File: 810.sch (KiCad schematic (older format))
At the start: 286 parts

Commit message: changed to Toshiba matched pairs, added 12dB/24dB selector switch
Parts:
- removed Q? (x2): PMP4201G, TO_SOT_Packages_SMD:SOT-353, symbol PMP4201G
- removed Q? (x2): PMP5201G, TO_SOT_Packages_SMD:SOT-353_SC-70-5, symbol PMP5201G
- added Q? (x2): 2SA1618, TO_SOT_Packages_SMD:SOT-353_SC-70-5, symbol 2SA1618
- added Q? (x2): 2SC4207, TO_SOT_Packages_SMD:SOT-353_SC-70-5, symbol 2SC4207
- added R?: 68K, MyModules:SM0603-R-JRL, symbol R_US
- added SW?: SPDT, symbol SPDT
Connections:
- wire segments 594 -> 596
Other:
- note added: "VCA"
- moved on the sheet: C?, J?, Q?, R?, SW?, TP?, U?, U?A, U?B, VR?

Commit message: gibber jabber
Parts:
- removed C?: 10μ, symbol CP_US
- removed U?: CD40106, Housings_SSOP:TSSOP-14_4.4x5mm_Pitch0.65mm, symbol CD40106
- added C?: 10μF, Capacitors_SMD:c_elec_5x5.3, symbol CP_US
- added J?: PJ301BM, symbol JACK_MONO_SW
- added U?: CD40106, Housings_SSOP:TSSOP-14_4.4x5mm_Pitch0.65mm, symbol CD40106
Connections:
- net +12V: now also U?.10 (J), U?.11 (K); no longer U?.5 (K), U?.6 (J)
- net GND: now also U?.11 (In), U?.13 (In), U?.5 (In), U?.9 (In), U?.9 (Sd), J?.1; no longer U?.1 (In), U?.1 (In), U?.1 (In), U?.1 (In), U?.7 (Sd), U?.8 (VSS)
- net VCO_PULSE: now also U?.12 (X0)
- net VCO_SAW: now also U?.14 (X1)
- net VCO_SINE: now also U?.11 (X3)
- net VCO_TRI: now also U?.15 (X2)
- net at C?.1, R?.1, U?.3 (-): now also C?.1 (+)
- net at R?.2, R?.2: now also C?.2 (-)
- net at U?.9 (B): now also U?.15 (Q); no longer U?.1 (Q)
- net at C?.1, R?.1, R?.1: now also U?.3 (In)
- net at U?.2 (~Q): now also U?.13 (Cp); no longer U?.3 (Cp)
- net at U?.3 (Cp): now also U?.4 (Out)
- net at U?.2 (Out), U?.4 (Cd): now also U?.12 (Cd); no longer U?.4 (Cd)
- net SYNC_IN: no longer names the net of R?.1
- net SYNC_IN: now also J?.3
- no-connect marks 24 -> 25
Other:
- note added: "00 PULSE\n01 SAW\n10 TRI\n11 SINE"
- note added: "SYNC"
- note removed: "00 LOW PASS 24 dB\n01 LOW PASS 12 dB\n10 BAND PASS 12 dB\n11 HIGH PASS 24 dB"
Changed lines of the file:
@@
 	0    -1   -1   0
 $EndComp
-Text GLabel 20275 5575 0    60   Input ~ 0
+Text GLabel 19975 5575 0    60   Input ~ 0
 VCO_TRI
 Text GLabel 20125 5275 0    60   Input ~ 0
 VCO_PULSE
-Text GLabel 20275 5725 0    60   Input ~ 0
+Text GLabel 20050 5725 0    60   Input ~ 0
 VCO_SINE
-Text GLabel 20175 5425 0    60   Input ~ 0
+Text GLabel 20025 5425 0    60   Input ~ 0
 VCO_SAW
 Text GLabel 21975 5275 2    60   Output ~ 0
@@
 	0    -1   -1   0
 $EndComp
-Text GLabel 1425 6875 0    60   Input ~ 0
-SYNC_IN
 Wire Wire Line
 	1900 6875 1950 6875
@@
 Wire Wire Line
 	2025 11975 2425 11975
-$Comp
-L CP_US C?
-U 1 1 596C3983
-P 3275 13125
-F 0 "C?" V 3350 12900 50  0000 L CNN
-F 1 "10μ" V 3350 13200 50  0000 L CNN
-F 2 "" H 3275 13125 60  0000 C CNN
-F 3 "" H 3275 13125 60  0000 C CNN
-	1    3275 13125
-	0    1    1    0
-$EndComp
 Wire Wire Line
 	4675 13225 5425 13225
@@
 $Comp
 L CD4027 U?
-U 1 1 596C393E
+U 2 1 596C393E
 P 23350 4575
 F 0 "U?" H 23550 4875 60  0000 C CNN
@@
 F 2 "Housings_SSOP:TSSOP-16_4.4x5mm_Pitch0.65mm" H 23350 4575 60  0001 C CNN
 F 3 "" H 23350 4575 60  0000 C CNN
-	1    23350 4575
+	2    23350 4575
 	-1   0    0    -1
 $EndComp
-Text Notes 22300 2975 0    60   ~ 0
-00 LOW PASS 24 dB\n01 LOW PASS 12 dB\n10 BAND PASS 12 dB\n11 HIGH PASS 24 dB
+Text Notes 22275 4100 0    60   ~ 0
+00 PULSE\n01 SAW\n10 TRI\n11 SINE
 $Comp
 L +12V #PWR?
@@
 $Comp
 L CD40106 U?
-U 1 1 596C3983
+U 2 1 596C3983
 P 26750 4575
 F 0 "U?" H 26850 4725 50  0000 L CNN
@@
 F 2 "Housings_SSOP:TSSOP-14_4.4x5mm_Pitch0.65mm" H 26750 4575 60  0001 C CNN
 F 3 "" H 26750 4575 60  0000 C CNN
-	1    26750 4575
+	2    26750 4575
 	-1   0    0    -1
 $EndComp
@@
 $Comp
 L CD40106 U?
-U 1 1 596C3991
+U 4 1 596C3991
 P 29625 3900
 F 0 "U?" H 29725 4050 50  0000 L CNN
@@
 F 2 "Housings_SSOP:TSSOP-14_4.4x5mm_Pitch0.65mm" H 29625 3900 60  0001 C CNN
 F 3 "" H 29625 3900 60  0000 C CNN
-	1    29625 3900
+	4    29625 3900
 	1    0    0    -1
 $EndComp
 $Comp
 L CD40106 U?
-U 1 1 596C3998
+U 5 1 596C3998
 P 29625 4600
 F 0 "U?" H 29725 4750 50  0000 L CNN
@@
 F 2 "Housings_SSOP:TSSOP-14_4.4x5mm_Pitch0.65mm" H 29625 4600 60  0001 C CNN
 F 3 "" H 29625 4600 60  0000 C CNN
-	1    29625 4600
+	5    29625 4600
 	1    0    0    -1
 $EndComp
 $Comp
 L CD40106 U?
-U 1 1 596C399F
+U 6 1 596C399F
 P 29625 5300
 F 0 "U?" H 29725 5450 50  0000 L CNN
@@
 F 2 "Housings_SSOP:TSSOP-14_4.4x5mm_Pitch0.65mm" H 29625 5300 60  0001 C CNN
 F 3 "" H 29625 5300 60  0000 C CNN
-	1    29625 5300
+	6    29625 5300
 	1    0    0    -1
 $EndComp
 $Comp
 L CD40106 U?
-U 1 1 596C39A6
+U 3 1 596C39A6
 P 29625 3250
 F 0 "U?" H 29725 3400 50  0000 L CNN
@@
 F 2 "Housings_SSOP:TSSOP-14_4.4x5mm_Pitch0.65mm" H 29625 3250 60  0001 C CNN
 F 3 "" H 29625 3250 60  0000 C CNN
-	1    29625 3250
+	3    29625 3250
 	1    0    0    -1
 $EndComp
@@
 Wire Wire Line
 	11725 14625 18850 14625
+$Comp
+L CP_US C?
+U 1 1 5971B5DE
+P 3275 13125
+F 0 "C?" V 3100 12925 50  0000 L CNN
+F 1 "10μF" V 3100 13150 50  0000 L CNN
+F 2 "Capacitors_SMD:c_elec_5x5.3" H 3275 13125 60  0001 C CNN
+F 3 "" H 3275 13125 60  0000 C CNN
+F 4 "UUQ1E100MCL1GB" V 3425 13225 60  0000 C CNN "Part Number"
+	1    3275 13125
+	0    1    1    0
+$EndComp
+Wire Wire Line
+	20125 5275 20350 5275
+Wire Wire Line
+	20025 5425 20350 5425
+Wire Wire Line
+	19975 5575 20350 5575
+Wire Wire Line
+	20050 5725 20350 5725
+$Comp
+L JACK_MONO_SW J?
+U 1 1 59733593
+P 1175 7025
+F 0 "J?" H 625 6925 60  0000 C CNN
+F 1 "PJ301BM" H 925 7225 60  0000 C CNN
+F 2 "" H 1075 7025 60  0000 C CNN
+F 3 "" H 1075 7025 60  0000 C CNN
+	1    1175 7025
+	1    0    0    1
+$EndComp
+$Comp
+L GND_R #PWR?
+U 1 1 59734986
+P 1425 7350
+F 0 "#PWR?" H 1425 7350 30  0001 C CNN
+F 1 "GND_R" H 1425 7250 30  0001 C CNN
+F 2 "" H 1425 7350 60  0000 C CNN
+F 3 "" H 1425 7350 60  0000 C CNN
+	1    1425 7350
+	1    0    0    -1
+$EndComp
+Wire Wire Line
+	1425 7175 1425 7350
+NoConn ~ 1425 7025
+Text Notes 900  6750 0    60   ~ 0
+SYNC
 $EndSCHEMATC

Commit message: finishing off, tidying up
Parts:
- removed SW?: DP6T-ROTARY-SWITCH, symbol DP6T-ROTARY-SWITCH
- added P?: CONN_01X08, Pin_Headers:Pin_Header_Angled_1x08_Pitch2.54mm, symbol CONN_01X08
- Q? (x2): footprint TO_SOT_Packages_SMD:SOT-353_SC-70-5 -> MyModules:SOT753_TSOP5_SC-74A
- SW?: value KS-01Q -> BF3-1050; footprint synth:KS-01Q-02-JRL -> MyModules:B3F-1050-OMRON
- VR?: footprint (none) -> MyModules:Bourns-3296W
- VR?: footprint (none) -> MyModules:RV16A-41-JRL
- VR?: footprint MyModules:TC33X-2 -> MyModules:Bourns-3296W
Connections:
- net +10V: now also R?.2, R?.2, VR?.1, VR?.3; no longer U?.8 (V+)
- net +12V: now also U?.8 (V+); no longer R?.2, R?.2, VR?.1, VR?.3
- net -10V: now also VR?.3; no longer U?.4 (V-)
- net -12V: now also U?.4 (V-); no longer VR?.3
- net GND: now also P?.6 (P6), P?.7 (P7)
- net at R?.1, VR?.1: now also P?.1 (P1)
- net at R?.1, R?.2: now also P?.2 (P2)
- net at R?.1, R?.2: now also P?.4 (P4)
- net at R?.1, R?.2: now also P?.5 (P5)
- net at R?.1, R?.2: now also P?.3 (P3)
- net at U?.1 (+): now also P?.8 (P8)
- net at VR?.2: now also R?.1
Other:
- note added: "Is additional DC\nblocking stage \nreally needed\nhere?"
- note added: "JP8 SYNC"
- note added: "ROTARY SWITCH\nGOES ON SUB BOARD"
- note added: "USE TOSHIBA\nNPN/PNP\nARRAY HERE?"

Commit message: added bi-color LED level indicator circuit
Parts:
- added C?: 0.047μF, symbol C_US
- added C?: 0.22µ, MyModules:SM0603-C-JRL, symbol C_US
- added D?: LED_BICOLOR, symbol LED_BICOLOR
- added D?: 1N4148, symbol D
- added R?: 100K, MyModules:SM0603-R-JRL, symbol R_US
- added R? (x2): 10K, MyModules:SM0603-R-JRL, symbol R_US
- added R?: 1meg, MyModules:SM0603-R-JRL, symbol R_US
- added R?: 1K, MyModules:SM0603-R-JRL, symbol R_US
- added R?: 51K, MyModules:SM0603-R-JRL, symbol R_US
- added R?: 68K, MyModules:SM0603-R-JRL, symbol R_US
- added R? (x2): 12K, MyModules:SM0603-R-JRL, symbol R_US
- added U? (x4): TL074-, symbol TL074-
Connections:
- net +12V: now also R?.2, U?.4 (V+)
- net -12V: now also U?.11 (V-)
- net GND: now also C?.2, D?.1, R?.1, R?.1, U?.12 (+)
- net at C?.2, R?.1, R?.2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: now also R?.1
- new net: D?.2 (A), U?.1
- new net: R?.1, U?.2 (-)
- new net: R?.2, U?.3 (+)
- new net: C?.1, R?.2, U?.14, U?.5 (+)
- new net: C?.2, R?.2, U?.13 (-)
- new net: C?.1, D?.1 (K), R?.2, R?.2, U?.6 (-)
- new net: R?.1, U?.7
- new net: R?.1, R?.1, U?.10 (+)
- new net: R?.1, R?.2, U?.8
- new net: R?.1, R?.2, U?.9 (-)
- new net: D?.2, R?.2
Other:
- note added: "810\n"
- note added: "Change divider\nfor 12V rails"
- moved on the sheet: C?, D?, F?, J?, P?, Q?, Q?A, Q?B, R?, SW?, TC?, TP?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

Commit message: annotated and ERC done
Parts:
- added J18: PJ301B, MyModules:PJ-301B-JACK-SLOTS, symbol JACK_MONO_SW
- gave numbers to parts that had none: 287
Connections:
- net GND: now also J18.1
- net OUT: no longer names the net of R113.2
- net OUT: now also J18.3
- no-connect marks 25 -> 27
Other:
- note added: "VCA OUT"
- note added: "VCF OUT"
- note added: "VCO OUT"

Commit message: pcbnew file created, pots/jacks/switches placed
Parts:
- C1, C11, C12, C14, C16, C17, C18, C22, C24, C26, C3, C4: footprint (none) -> MyModules:SM0603-C-JRL
- C15, C2, C20, C23, C45, C46: footprint Capacitors_SMD:c_elec_5x5.3 -> MyModules:jrl_c_elec_5x5.3
- C21: footprint (none) -> MyModules:jrl_c_elec_4x5.3
- D1, D2, D4, Q6: footprint (none) -> MyModules:SOT23-132-JRL
- D14, D3, D5, D6, D7, D8, D9: footprint (none) -> MyModules:SOD323-C1A2
- D15: footprint (none) -> Pin_Headers:Pin_Header_Straight_1x03_Pitch2.00mm
- J1, J10, J11, J12, J13, J14, J15, J16, J2, J3, J6, J7, J8, J9: footprint (none) -> MyModules:PJ-301B-JACK-SLOTS
- P2: footprint Pin_Headers:Pin_Header_Straight_2x05 -> Pin_Headers:Pin_Header_Straight_2x05_Pitch2.54mm
- Q1, Q11, Q12, Q13, Q14, Q7, Q8: footprint SOT-23 -> TO_SOT_Packages_SMD:SOT-23
- Q3, Q4: footprint MyModules:SOT753_TSOP5_SC-74A -> TO_SOT_Packages_SMD:SOT-353_SC-70-5
- R1, R12, R2, R6, R7: footprint (none) -> MyModules:SM0603-R-JRL
- SW1, SW2: footprint (none) -> MyModules:SS-12F108-1P2T-SLIDE
- TC1: footprint (none) -> MyModules:SM0805-HAND
- TP2, TP3, TP4: footprint (none) -> MyModules:TEST POINT
- U10: footprint (none) -> MyModules:TSSOP8-JRL
- U11: footprint (none) -> Housings_SSOP:TSSOP-14_4.4x5mm_Pitch0.65mm
- U12, U13, U14, U15, U16, U18: footprint (none) -> MyModules:SOT753_TSOP5_SC-74A
- VR1, VR10, VR15, VR17, VR18, VR19, VR2, VR20, VR21, VR22, VR26, VR9: footprint (none) -> MyModules:R0904N-SONG-HUEI
- VR11, VR14, VR16, VR23, VR24, VR25, VR27, VR3: footprint (none) -> MyModules:TC33X-2
- VR4, VR5, VR6, VR8: footprint MyModules:RV16A-41-JRL -> MyModules:R0904N-SONG-HUEI

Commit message: added hard/soft sync switch
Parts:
- added P3: CONN_01X03, Pin_Headers:Pin_Header_Straight_1x03_Pitch2.54mm, symbol CONN_01X03
- added P4: CONN_01X08, Pin_Headers:Pin_Header_Angled_1x08_Pitch2.54mm, symbol CONN_01X08
- added R135: 15K, MyModules:SM0603-R-JRL, symbol R_US
- added SW4: SPDT, MyModules:SS-12F108-1P2T-SLIDE, symbol SPDT
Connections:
- net -12V: now also P3.3 (P3); no longer D3.2 (A), Q1.2 (E), R8.1
- net GND: now also P3.1 (P1)
- net SYNC: now also R135.2, SW4.1 (A); no longer Q1.3 (C)
- new net: D3.2 (A), P3.2 (P2), Q1.2 (E), R8.1
- new net: Q1.3 (C), R135.1, SW4.2 (B)
- no-connect marks 27 -> 36
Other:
- note added: "-12V for JP8 sync\nGND for M-112 sync"
- note added: "STRONG"
- note added: "WEAK"
- moved on the sheet: C1, D3, J1, Q1, R5, R8

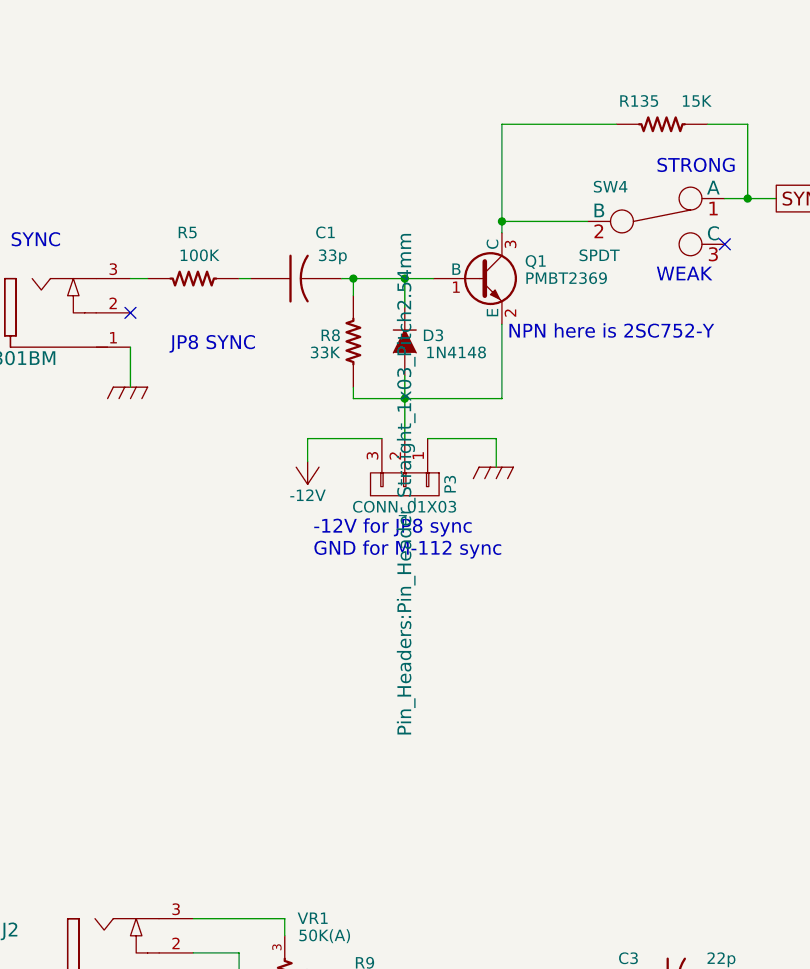
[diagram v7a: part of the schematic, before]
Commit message: updated SW1 rotary switch footprint to Alpha SR2511
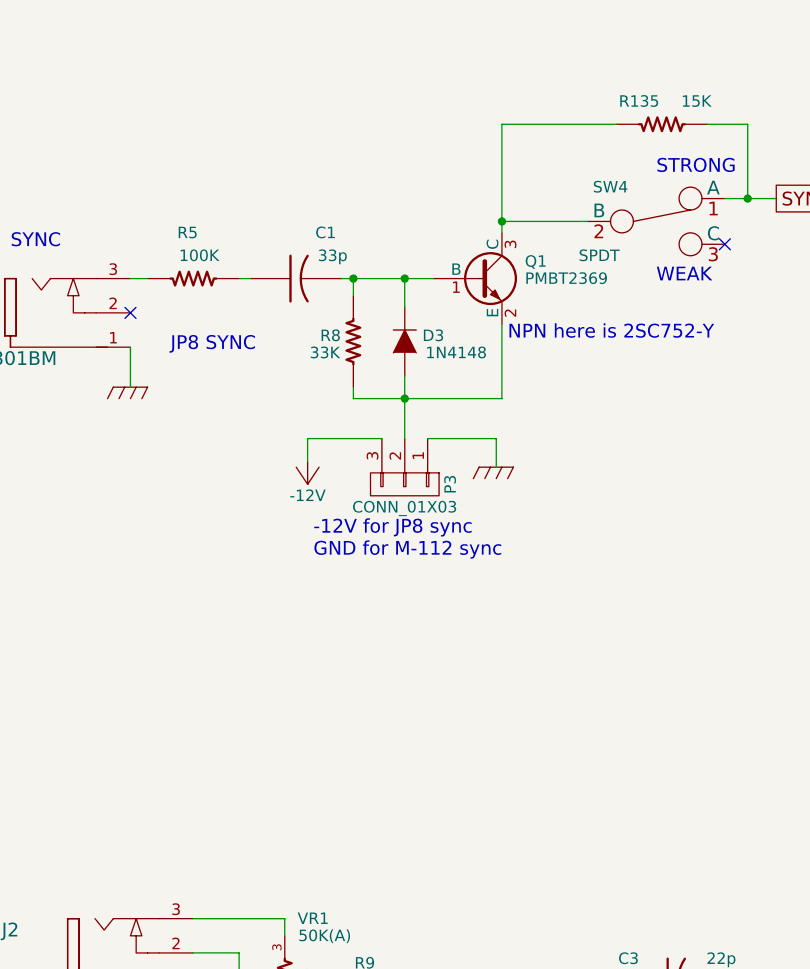
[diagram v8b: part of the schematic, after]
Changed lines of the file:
@@
 F 0 "P3" H 2950 8100 50  0000 C CNN
 F 1 "CONN_01X03" V 3050 7900 50  0000 C CNN
-F 2 "Pin_Headers:Pin_Header_Straight_1x03_Pitch2.54mm" H 2950 7900 60  0000 C CNN
+F 2 "Pin_Headers:Pin_Header_Straight_1x03_Pitch2.54mm" H 2950 7900 60  0001 C CNN
 F 3 "" H 2950 7900 60  0000 C CNN
 	1    2950 7900
